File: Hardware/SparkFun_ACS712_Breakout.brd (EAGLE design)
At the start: 24.1 x 15.2 mm, 12 parts

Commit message: Fixed ENG github issues
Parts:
- renumbered U$1 to JP7
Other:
- board text added: "V12"
- board text removed: "V01"
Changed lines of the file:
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@@
 <text x="7.4676" y="2.8956" size="1.016" layer="21" font="vector" ratio="15">ACS712 </text>
 <text x="6.731" y="1.4986" size="1.016" layer="21" font="vector" ratio="15">Breakout</text>
-<text x="21.082" y="0.5842" size="1.016" layer="16" font="vector" ratio="15" rot="MR0">V01</text>
+<text x="21.082" y="0.5842" size="1.016" layer="16" font="vector" ratio="15" rot="MR0">V12</text>
 <dimension x1="-3.81" y1="0" x2="-3.81" y2="15.24" x3="-6.35" y3="7.62" textsize="1.778" textratio="15" layer="47" unit="inch"/>
 <dimension x1="-2.54" y1="19.05" x2="21.59" y2="19.05" x3="9.525" y3="20.32" textsize="1.778" textratio="15" layer="47" unit="inch"/>
@@
 <text x="8.3566" y="-12.7508" size="1.778" layer="51" font="vector">Pete Dokter</text>
 <text x="-10.16" y="-15.5194" size="1.778" layer="51" font="vector">Revised by: Patrick Alberts</text>
+<text x="16.5354" y="11.8872" size="0.8128" layer="22" font="vector" ratio="15" rot="MR180">VCC</text>
+<text x="18.923" y="9.271" size="0.8128" layer="21" font="vector" ratio="15" rot="R180">VOUT</text>
+<text x="15.748" y="9.271" size="0.8128" layer="22" font="vector" ratio="15" rot="MR180">VOUT</text>
+<text x="18.9484" y="6.731" size="0.8128" layer="21" font="vector" ratio="15" rot="R180">FILT</text>
+<text x="15.9766" y="6.731" size="0.8128" layer="22" font="vector" ratio="15" rot="MR180">FILT</text>
+<text x="16.4338" y="4.191" size="0.8128" layer="22" font="vector" ratio="15" rot="MR180">GND</text>
 </plain>
 <attributes>
@@
 </autorouter>
 <elements>
-<element name="U$1" library="SparkFun-AnalogIC" package="SO08" value="ACS712" x="10.287" y="7.62" rot="R270">
+<element name="JP7" library="SparkFun-AnalogIC" package="SO08" value="ACS712" x="10.287" y="7.62" rot="R270">
 <attribute name="PROD_ID" value="IC-08964" x="10.287" y="7.62" size="1.778" layer="27" rot="R270" display="off"/>
 </element>
@@
 <signal name="N$1">
 <contactref element="JP1" pad="P$1"/>
-<contactref element="U$1" pad="1"/>
-<contactref element="U$1" pad="2"/>
+<contactref element="JP7" pad="1"/>
+<contactref element="JP7" pad="2"/>
 <wire x1="1.27" y1="11.43" x2="2.413" y2="11.43" width="1.778" layer="1"/>
 <wire x1="2.413" y1="11.43" x2="4.953" y2="8.89" width="1.778" layer="1"/>
@@
 </signal>
 <signal name="N$3">
-<contactref element="U$1" pad="3"/>
+<contactref element="JP7" pad="3"/>
 <contactref element="JP2" pad="P$1"/>
-<contactref element="U$1" pad="4"/>
+<contactref element="JP7" pad="4"/>
 <wire x1="1.27" y1="3.81" x2="2.413" y2="3.81" width="1.778" layer="1"/>
 <wire x1="2.413" y1="3.81" x2="4.953" y2="6.35" width="1.778" layer="1"/>
@@
 </signal>
 <signal name="VCC">
-<contactref element="U$1" pad="8"/>
+<contactref element="JP7" pad="8"/>
 <contactref element="JP3" pad="1"/>
 <wire x1="12.9032" y1="9.525" x2="18.415" y2="9.525" width="0.254" layer="1"/>
@@
 <signal name="VOUT">
 <contactref element="JP3" pad="2"/>
-<contactref element="U$1" pad="7"/>
+<contactref element="JP7" pad="7"/>
 <wire x1="19.177" y1="8.89" x2="20.32" y2="8.89" width="0.254" layer="1"/>
 <wire x1="18.542" y1="8.255" x2="19.177" y2="8.89" width="0.254" layer="1"/>
@@
 </signal>
 <signal name="FILT">
-<contactref element="U$1" pad="6"/>
+<contactref element="JP7" pad="6"/>
 <contactref element="JP3" pad="3"/>
 <contactref element="C1" pad="1"/>
-<wire x1="12.9032" y1="6.985" x2="15.5076" y2="6.985" width="0.254" layer="1"/>
-<wire x1="15.3416" y1="7.0222" x2="19.6478" y2="7.0222" width="0.254" layer="1"/>
 <wire x1="19.6478" y1="7.0222" x2="20.32" y2="6.35" width="0.254" layer="1"/>
-<wire x1="15.5076" y1="6.985" x2="15.3416" y2="7.0222" width="0" layer="19" extent="1-1"/>
+<wire x1="19.6478" y1="7.0222" x2="15.3416" y2="7.0222" width="0.254" layer="1"/>
+<wire x1="12.9032" y1="6.985" x2="15.3044" y2="6.985" width="0.254" layer="1"/>
+<wire x1="15.3044" y1="6.985" x2="15.3416" y2="7.0222" width="0.254" layer="1"/>
 </signal>
 <signal name="GND">
@@
 <vertex x="10.9474" y="15.24"/>
 </polygon>
-<contactref element="U$1" pad="5"/>
-<contactref element="JP3" pad="4"/>
+<contactref element="JP7" pad="5"/>
 <contactref element="C1" pad="2"/>
 <via x="15.24" y="1.27" extent="1-16" drill="0.508"/>
+<contactref element="JP3" pad="4"/>
 </signal>
 </signals>

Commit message: Fixed sch
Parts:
- moved FRAME1 2.84 mm to (-22.9, -10.2)
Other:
- board text added: "Max Current 2.1kV"
- board text removed: "All units are in inches"
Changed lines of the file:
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@@
 <text x="6.731" y="1.4986" size="1.016" layer="21" font="vector" ratio="15">Breakout</text>
 <text x="21.082" y="0.5842" size="1.016" layer="16" font="vector" ratio="15" rot="MR0">V12</text>
-<dimension x1="-3.81" y1="0" x2="-3.81" y2="15.24" x3="-6.35" y3="7.62" textsize="1.778" textratio="15" layer="47" unit="inch"/>
-<dimension x1="-2.54" y1="19.05" x2="21.59" y2="19.05" x3="9.525" y3="20.32" textsize="1.778" textratio="15" layer="47" unit="inch"/>
-<text x="-2.54" y="16.51" size="1.27" layer="47" font="vector" ratio="15">All units are in inches</text>
-<text x="8.3566" y="-12.7508" size="1.778" layer="51" font="vector">Pete Dokter</text>
-<text x="-10.16" y="-15.5194" size="1.778" layer="51" font="vector">Revised by: Patrick Alberts</text>
-<text x="16.5354" y="11.8872" size="0.8128" layer="22" font="vector" ratio="15" rot="MR180">VCC</text>
+<dimension x1="-3.81" y1="0" x2="-3.81" y2="15.24" x3="-6.35" y3="7.62" textsize="1.778" textratio="15" layer="47" unit="inch" visible="yes"/>
+<dimension x1="-2.54" y1="19.05" x2="21.59" y2="19.05" x3="9.525" y3="20.32" textsize="1.778" textratio="15" layer="47" unit="inch" visible="yes"/>
+<text x="7.0866" y="-10.2108" size="1.778" layer="51" font="vector">Pete Dokter</text>
+<text x="-11.43" y="-12.9794" size="1.778" layer="51" font="vector">Revised by: Patrick Alberts</text>
+<text x="16.49221875" y="11.877040625" size="0.8128" layer="22" font="vector" ratio="15" rot="MR180">VCC</text>
 <text x="18.923" y="9.271" size="0.8128" layer="21" font="vector" ratio="15" rot="R180">VOUT</text>
-<text x="15.748" y="9.271" size="0.8128" layer="22" font="vector" ratio="15" rot="MR180">VOUT</text>
-<text x="18.9484" y="6.731" size="0.8128" layer="21" font="vector" ratio="15" rot="R180">FILT</text>
-<text x="15.9766" y="6.731" size="0.8128" layer="22" font="vector" ratio="15" rot="MR180">FILT</text>
-<text x="16.4338" y="4.191" size="0.8128" layer="22" font="vector" ratio="15" rot="MR180">GND</text>
+<text x="15.7607" y="9.260840625" size="0.8128" layer="22" font="vector" ratio="15" rot="MR180">VOUT</text>
+<text x="16.0426375" y="6.733540625" size="0.8128" layer="22" font="vector" ratio="15" rot="MR180">FILT</text>
+<text x="16.46428125" y="4.193540625" size="0.8128" layer="22" font="vector" ratio="15" rot="MR180">GND</text>
+<text x="4.318" y="0.381" size="0.8128" layer="21" font="vector" ratio="15">Max Current 2.1kV </text>
 </plain>
 <attributes>
@@
 <element name="JP4" library="SparkFun" package="MICRO-FIDUCIAL" value="FIDUCIALUFIDUCIAL" x="20.32" y="13.97"/>
 <element name="JP5" library="SparkFun" package="MICRO-FIDUCIAL" value="FIDUCIALUFIDUCIAL" x="-1.651" y="1.016"/>
-<element name="FRAME1" library="SparkFun-Aesthetics" package="CREATIVE_COMMONS" value="" x="-21.61245625" y="-12.7">
-<attribute name="VERSION" value="v01" x="-21.61245625" y="-12.7" size="1.778" layer="27" display="off"/>
-<attribute name="DESIGNER" value="NAME" x="-21.61245625" y="-12.7" size="1.778" layer="27" display="off"/>
+<element name="FRAME1" library="SparkFun-Aesthetics" package="CREATIVE_COMMONS" value="" x="-22.88245625" y="-10.16">
+<attribute name="VERSION" value="v01" x="-22.88245625" y="-10.16" size="1.778" layer="27" display="off"/>
+<attribute name="DESIGNER" value="NAME" x="-22.88245625" y="-10.16" size="1.778" layer="27" display="off"/>
 </element>
 <element name="JP6" library="SparkFun-Connectors" package="1X02_NO_SILK" value="" x="5.207" y="6.35" rot="R90"/>
@@
 <contactref element="JP7" pad="5"/>
 <contactref element="C1" pad="2"/>
-<via x="15.24" y="1.27" extent="1-16" drill="0.508"/>
+<via x="15.494" y="2.413" extent="1-16" drill="0.508"/>
 <contactref element="JP3" pad="4"/>
 </signal>

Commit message: Fixed qc issues
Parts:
- renumbered JP7 to U1
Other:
- board text removed: "Max Current 2.1kV"
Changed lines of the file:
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@@
 <layer number="47" name="Measures" color="7" fill="1" visible="no" active="yes"/>
 <layer number="48" name="Document" color="7" fill="1" visible="no" active="yes"/>
-<layer number="49" name="Reference" color="7" fill="1" visible="no" active="yes"/>
+<layer number="49" name="Reference" color="7" fill="1" visible="yes" active="yes"/>
 <layer number="50" name="dxf" color="7" fill="1" visible="no" active="yes"/>
 <layer number="51" name="tDocu" color="6" fill="1" visible="yes" active="yes"/>
@@
 <board>
 <plain>
-<wire x1="-2.54" y1="0" x2="-2.54" y2="15.24" width="0.254" layer="20"/>
-<wire x1="-2.54" y1="15.24" x2="21.59" y2="15.24" width="0.254" layer="20"/>
-<wire x1="21.59" y1="15.24" x2="21.59" y2="0" width="0.254" layer="20"/>
-<wire x1="21.59" y1="0" x2="-2.54" y2="0" width="0.254" layer="20"/>
+<wire x1="-2.54" y1="0" x2="-2.54" y2="15.24" width="0.2032" layer="20"/>
+<wire x1="-2.54" y1="15.24" x2="21.59" y2="15.24" width="0.2032" layer="20"/>
+<wire x1="21.59" y1="15.24" x2="21.59" y2="0" width="0.2032" layer="20"/>
+<wire x1="21.59" y1="0" x2="-2.54" y2="0" width="0.2032" layer="20"/>
 <text x="18.8976" y="11.8872" size="0.8128" layer="21" font="vector" ratio="15" rot="R180">VCC</text>
 <text x="18.923" y="9.271" size="0.8128" layer="21" font="vector" ratio="15" rot="R180">VOUT</text>
@@
 <text x="16.0426375" y="6.733540625" size="0.8128" layer="22" font="vector" ratio="15" rot="MR180">FILT</text>
 <text x="16.46428125" y="4.193540625" size="0.8128" layer="22" font="vector" ratio="15" rot="MR180">GND</text>
-<text x="4.318" y="0.381" size="0.8128" layer="21" font="vector" ratio="15">Max Current 2.1kV </text>
 </plain>
 <attributes>
@@
 </autorouter>
 <elements>
-<element name="JP7" library="SparkFun-AnalogIC" package="SO08" value="ACS712" x="10.287" y="7.62" rot="R270">
+<element name="U1" library="SparkFun-AnalogIC" package="SO08" value="ACS712" x="10.287" y="7.62" rot="R270">
 <attribute name="PROD_ID" value="IC-08964" x="10.287" y="7.62" size="1.778" layer="27" rot="R270" display="off"/>
 </element>
@@
 <signal name="N$1">
 <contactref element="JP1" pad="P$1"/>
-<contactref element="JP7" pad="1"/>
-<contactref element="JP7" pad="2"/>
+<contactref element="U1" pad="1"/>
+<contactref element="U1" pad="2"/>
 <wire x1="1.27" y1="11.43" x2="2.413" y2="11.43" width="1.778" layer="1"/>
 <wire x1="2.413" y1="11.43" x2="4.953" y2="8.89" width="1.778" layer="1"/>
@@
 </signal>
 <signal name="N$3">
-<contactref element="JP7" pad="3"/>
+<contactref element="U1" pad="3"/>
 <contactref element="JP2" pad="P$1"/>
-<contactref element="JP7" pad="4"/>
+<contactref element="U1" pad="4"/>
 <wire x1="1.27" y1="3.81" x2="2.413" y2="3.81" width="1.778" layer="1"/>
 <wire x1="2.413" y1="3.81" x2="4.953" y2="6.35" width="1.778" layer="1"/>
@@
 </signal>
 <signal name="VCC">
-<contactref element="JP7" pad="8"/>
+<contactref element="U1" pad="8"/>
 <contactref element="JP3" pad="1"/>
 <wire x1="12.9032" y1="9.525" x2="18.415" y2="9.525" width="0.254" layer="1"/>
@@
 <signal name="VOUT">
 <contactref element="JP3" pad="2"/>
-<contactref element="JP7" pad="7"/>
+<contactref element="U1" pad="7"/>
 <wire x1="19.177" y1="8.89" x2="20.32" y2="8.89" width="0.254" layer="1"/>
 <wire x1="18.542" y1="8.255" x2="19.177" y2="8.89" width="0.254" layer="1"/>
@@
 </signal>
 <signal name="FILT">
-<contactref element="JP7" pad="6"/>
+<contactref element="U1" pad="6"/>
 <contactref element="JP3" pad="3"/>
 <contactref element="C1" pad="1"/>
@@
 <vertex x="10.9474" y="15.24"/>
 </polygon>
-<contactref element="JP7" pad="5"/>
+<contactref element="U1" pad="5"/>
 <contactref element="C1" pad="2"/>
 <via x="15.494" y="2.413" extent="1-16" drill="0.508"/>

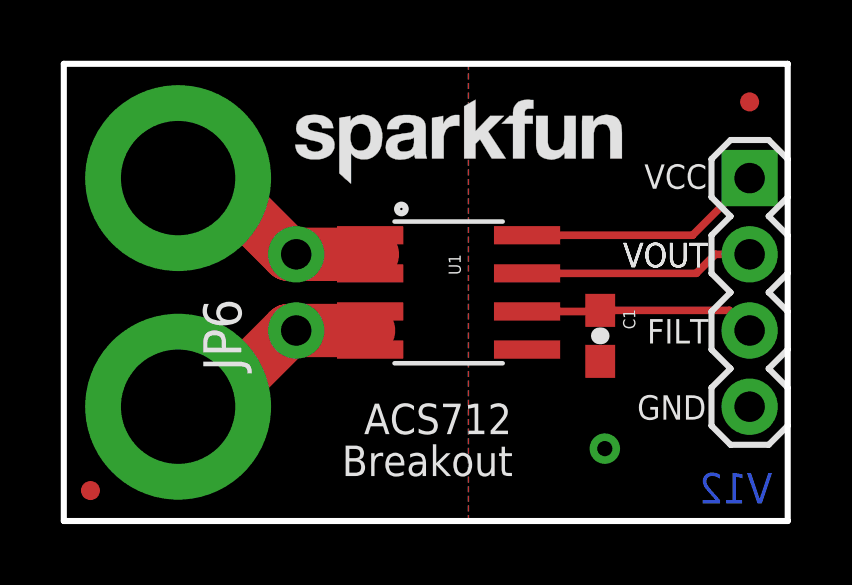
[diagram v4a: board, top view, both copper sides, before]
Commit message: Upped Trace width, fixed grid issue
upped to 90 mil

bo headers and sense headers are now on grid
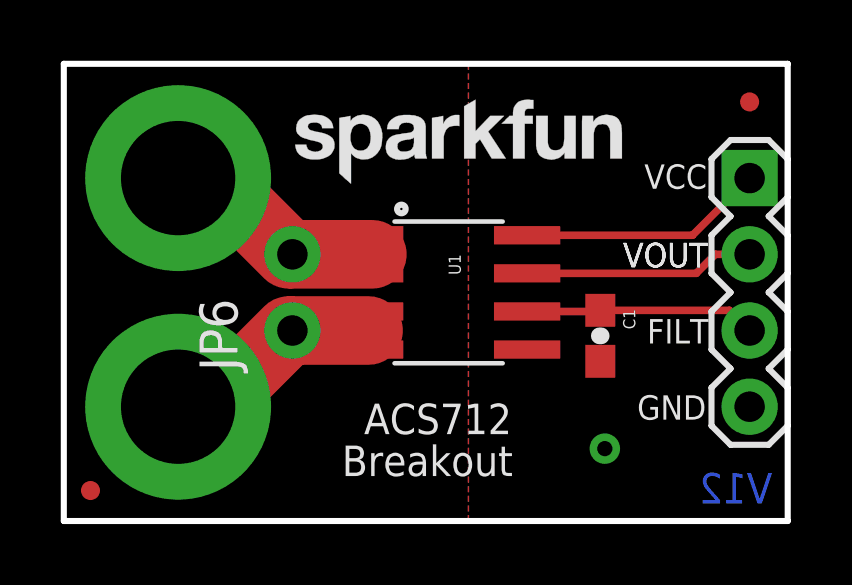
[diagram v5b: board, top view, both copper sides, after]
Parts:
- moved JP6 0.13 mm to (5.08, 6.35)
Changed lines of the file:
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@@
 <layer number="47" name="Measures" color="7" fill="1" visible="no" active="yes"/>
 <layer number="48" name="Document" color="7" fill="1" visible="no" active="yes"/>
-<layer number="49" name="Reference" color="7" fill="1" visible="yes" active="yes"/>
+<layer number="49" name="Reference" color="7" fill="1" visible="no" active="yes"/>
 <layer number="50" name="dxf" color="7" fill="1" visible="no" active="yes"/>
 <layer number="51" name="tDocu" color="6" fill="1" visible="yes" active="yes"/>
@@
 <attribute name="DESIGNER" value="NAME" x="-22.88245625" y="-10.16" size="1.778" layer="27" display="off"/>
 </element>
-<element name="JP6" library="SparkFun-Connectors" package="1X02_NO_SILK" value="" x="5.207" y="6.35" rot="R90"/>
+<element name="JP6" library="SparkFun-Connectors" package="1X02_NO_SILK" value="" x="5.08" y="6.35" rot="R90"/>
 <element name="LOGO2" library="SparkFun-Aesthetics" package="SFE_LOGO_FLAME_.3" value="SFE_LOGO_FLAME.3_INCH" x="12.7762" y="3.556" rot="MR0"/>
 <element name="C1" library="SparkFun-Capacitors" package="0603-CAP" value="1nF" x="15.3416" y="6.1722" rot="R270">
@@
 <contactref element="U1" pad="1"/>
 <contactref element="U1" pad="2"/>
-<wire x1="1.27" y1="11.43" x2="2.413" y2="11.43" width="1.778" layer="1"/>
-<wire x1="2.413" y1="11.43" x2="4.953" y2="8.89" width="1.778" layer="1"/>
-<wire x1="4.953" y1="8.89" x2="5.207" y2="8.89" width="1.778" layer="1"/>
-<wire x1="5.207" y1="8.89" x2="7.747" y2="8.89" width="1.778" layer="1"/>
+<wire x1="1.27" y1="11.43" x2="2.413" y2="11.43" width="2.286" layer="1"/>
+<wire x1="2.413" y1="11.43" x2="4.953" y2="8.89" width="2.286" layer="1"/>
+<wire x1="4.953" y1="8.89" x2="5.08" y2="8.89" width="1.778" layer="1"/>
+<wire x1="5.08" y1="8.89" x2="7.747" y2="8.89" width="2.286" layer="1"/>
 <wire x1="7.6708" y1="8.9662" x2="7.6708" y2="9.525" width="0.254" layer="1"/>
 <wire x1="7.747" y1="8.89" x2="7.6708" y2="8.9662" width="0.254" layer="1"/>
@@
 <contactref element="JP2" pad="P$1"/>
 <contactref element="U1" pad="4"/>
-<wire x1="1.27" y1="3.81" x2="2.413" y2="3.81" width="1.778" layer="1"/>
-<wire x1="2.413" y1="3.81" x2="4.953" y2="6.35" width="1.778" layer="1"/>
-<wire x1="4.953" y1="6.35" x2="5.207" y2="6.35" width="1.778" layer="1"/>
-<wire x1="5.207" y1="6.35" x2="7.62" y2="6.35" width="1.778" layer="1"/>
+<wire x1="1.27" y1="3.81" x2="2.413" y2="3.81" width="2.286" layer="1"/>
+<wire x1="2.413" y1="3.81" x2="4.953" y2="6.35" width="2.286" layer="1"/>
+<wire x1="4.953" y1="6.35" x2="5.08" y2="6.35" width="1.778" layer="1"/>
+<wire x1="5.08" y1="6.35" x2="7.62" y2="6.35" width="2.286" layer="1"/>
 <wire x1="7.6708" y1="6.2992" x2="7.6708" y2="5.715" width="0.254" layer="1"/>
 <wire x1="7.62" y1="6.35" x2="7.6708" y2="6.2992" width="0.254" layer="1"/>
